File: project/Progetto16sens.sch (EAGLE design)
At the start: 148 parts, among them IC1 LMZ14202TZE-ADJ_NOPB, J2 455-1750-1-ND, M1 43650-0201, M2 43650-0201, M3 43650-0201, M4 43650-0201, M5 ARDUINO-PRO-MINI, SW1 TL32PO, SW2 TL32PO, SW3 TL32PO

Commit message: turned in elaborato
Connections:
- removed net N$1: CB2.1, RB2.2, S5.OUT, S6.VCC, S7.OUT, S8.VCC
- removed net N$2: CB1.1, RB1.2, S1.OUT, S2.VCC, S3.OUT, S4.VCC
- removed net N$3: CB3.1, RB3.2, S10.VCC, S11.OUT, S12.VCC, S9.OUT
- removed net N$4: CB4.1, RB4.2, S13.OUT, S14.VCC, S15.OUT, S16.VCC
- removed net N$69: SV1.12, SV3.10, SV6.11, U$1.GND, U$1.GND_1, U$1.GND_2
- new net PWR_B1: CB1.1, RB1.2, S1.VCC, S2.VCC, S3.VCC, S4.VCC
- new net PWR_B2: CB2.1, RB2.2, S5.VCC, S6.VCC, S7.VCC, S8.VCC
- new net PWR_B3: CB3.1, RB3.2, S10.VCC, S11.VCC, S12.VCC, S9.VCC
- new net PWR_B4: CB4.1, RB4.2, S13.VCC, S14.VCC, S15.VCC, S16.VCC
- net B1: now also S1.OUT; no longer S1.VCC
- net B11: now also S11.OUT; no longer S11.VCC
- net B13: now also S13.OUT; no longer S13.VCC
- net B15: now also S15.OUT; no longer S15.VCC
- net B3: now also S3.OUT; no longer S3.VCC
- net B5: now also S5.OUT; no longer S5.VCC
- net B7: now also S7.OUT; no longer S7.VCC
- net B9: now also S9.OUT; no longer S9.VCC
- net GND: now also SV1.12, SV3.10, SV6.11, U$1.GND, U$1.GND_1, U$1.GND_2
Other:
- moved on the sheet: S1, S11, S13, S15, S3, S5, S7, S9

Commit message: continuing brd
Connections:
- removed net N$13: L_SW2.A, R_SW2.1
- removed net N$15: R_SW2.2, SW2.S
- removed net N$16: L_SW3.A, R_SW3.1
- removed net N$17: R_SW3.2, SW3.S
- removed net N$5: L_SW1.A, R_SW1.1
- removed net N$8: R_SW1.2, SW1.S
- removed net N$81: J1.6, M5.VCC
- new net N$1: L_SW2.C, R_SW2.2
- new net N$2: L_SW1.C, R_SW1.2
- new net N$3: L_SW3.C, R_SW3.2
- net +3V3: now also J1.6, M5.VCC, SW1.S, SW2.S, SW3.S; no longer L_SW1.C, L_SW2.C, L_SW3.C
- net GND: now also R_SW1.1, R_SW2.1, R_SW3.1
- net SW1: now also L_SW1.A
- net SW2: now also L_SW2.A
- net SW3: now also L_SW3.A
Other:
- moved on the sheet: L_SW1, L_SW2, L_SW3, R_SW1, R_SW2, R_SW3, SW1, SW2, SW3

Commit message: halfway done with wiring SEE WIRESTUB ERROR
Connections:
- removed net N$116: J2.2, M5.A6
- removed net N$117: J2.3, M5.A7
- removed net N$61: R_BALL.2, SW_BALL.O
- new net BX: J1.11, M5.D13
- net B1: now also BALL_MUX.I7, J2.3, M5.A7; no longer BALL_MUX.I0, J1.1, M5.A5
- net B10: now also BALL_MUX.I14, M5.D2, SV4.8; no longer BALL_MUX.I9, M5.D9, SV4.1
- net B11: now also BALL_MUX.I13, J1.10, M5.A0; no longer BALL_MUX.I10
- net B12: now also BALL_MUX.I12, J1.9, M5.A1; no longer BALL_MUX.I11, J1.7, M5.A3
- net B13: now also BALL_MUX.I11; no longer BALL_MUX.I12
- net B14: now also BALL_MUX.I10, J1.7, M5.A3; no longer BALL_MUX.I13, J1.9, M5.A1
- net B15: now also BALL_MUX.I9, J1.1, M5.A5; no longer BALL_MUX.I14, J1.10, M5.A0
- net B16: now also BALL_MUX.I8, J1.2, M5.A4; no longer BALL_MUX.I15, J1.11, M5.D13
- net B2: now also BALL_MUX.I6, J2.2, M5.A6; no longer BALL_MUX.I1, J1.2, M5.A4
- net B3: now also BALL_MUX.I5, M5.D9, SV4.1; no longer BALL_MUX.I2, M5.D2, SV4.8
- net B4: now also BALL_MUX.I4, M5.D8, SV4.2; no longer BALL_MUX.I3, M5.D3, SV4.7
- net B5: now also BALL_MUX.I3, M5.D7, SV4.3; no longer BALL_MUX.I4, M5.D4, SV4.6
- net B6: now also BALL_MUX.I2, M5.D6, SV4.4; no longer BALL_MUX.I5, M5.D5, SV4.5
- net B7: now also BALL_MUX.I1, M5.D5, SV4.5; no longer BALL_MUX.I6, M5.D6, SV4.4
- net B8: now also BALL_MUX.I0, M5.D4, SV4.6; no longer BALL_MUX.I7, M5.D7, SV4.3
- net B9: now also BALL_MUX.I15, M5.D3, SV4.7; no longer BALL_MUX.I8, M5.D8, SV4.2
- net E_IN: now also SV6.3, U$1.17/A3/TX4/SDA1; no longer SV6.2, U$1.16/A2/RX4/SCL1
- net E_OUT: now also SV6.2, U$1.16/A2/RX4/SCL1; no longer SV6.3, U$1.17/A3/TX4/SDA1
- net N_IN: now also SV6.5, U$1.19/A5/SCL; no longer SV6.4, U$1.18/A4/SDA
- net N_OUT: now also SV6.4, U$1.18/A4/SDA; no longer SV6.5, U$1.19/A5/SCL
- net S_IN: now also SV6.1, U$1.15/A1/TX3; no longer SV3.12, U$1.14/A0/TX3
- net S_OUT: now also SV3.12, U$1.14/A0/TX3; no longer SV6.1, U$1.15/A1/TX3
- net W_IN: now also SV3.9, U$1.41/A17; no longer SV3.8, U$1.40/A16
- net W_OUT: now also SV3.8, U$1.40/A16; no longer SV3.9, U$1.41/A17

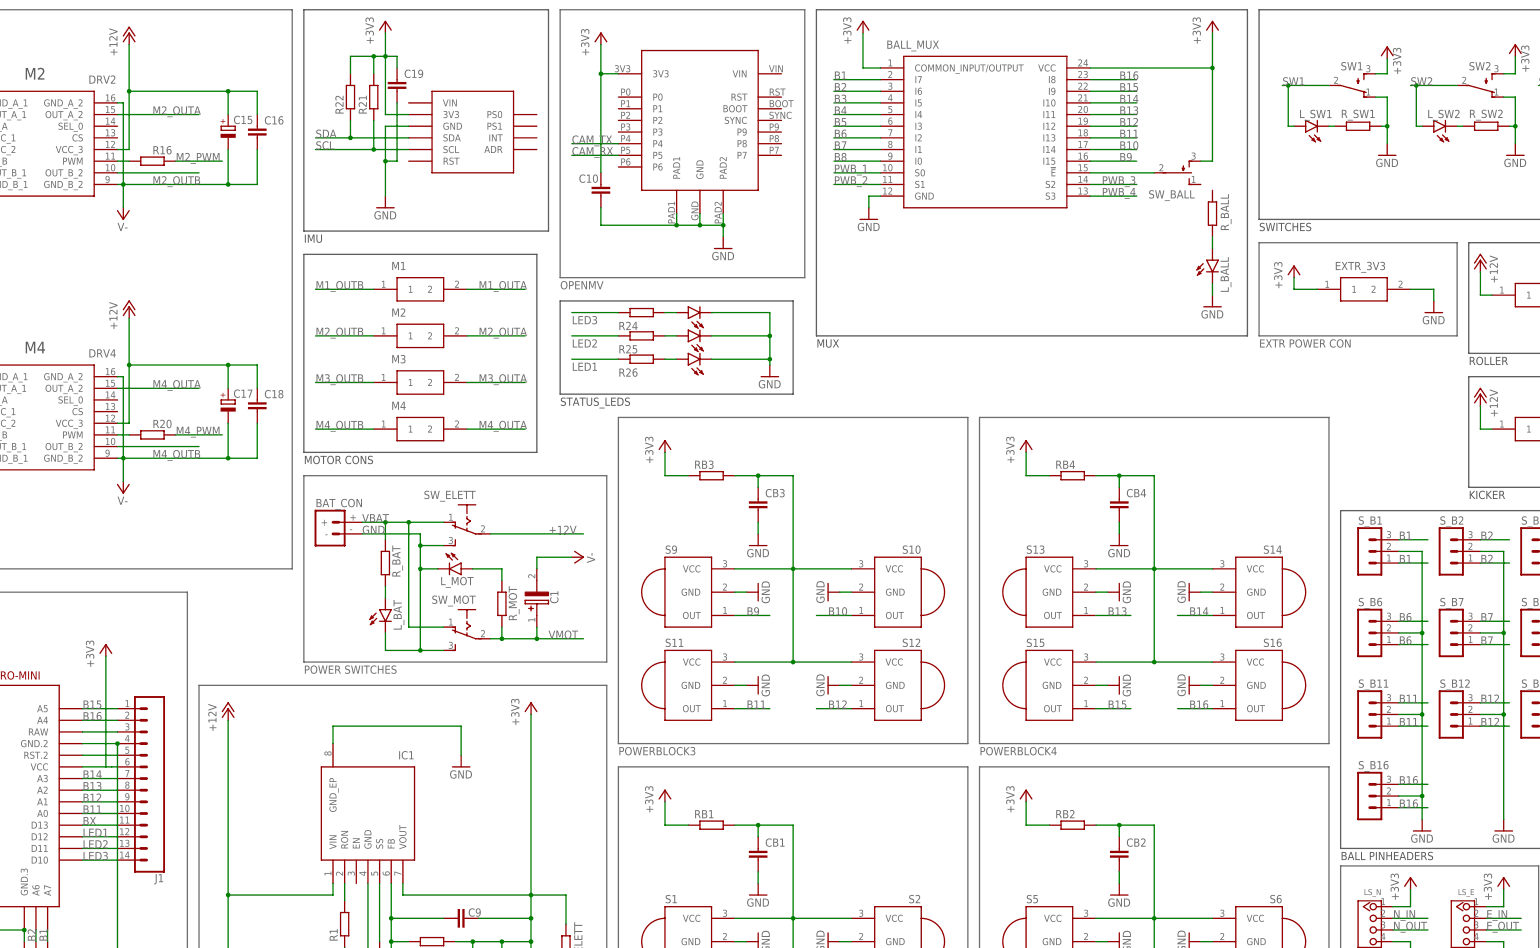
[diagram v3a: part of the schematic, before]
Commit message: elaborato almost done, board needs some fixing
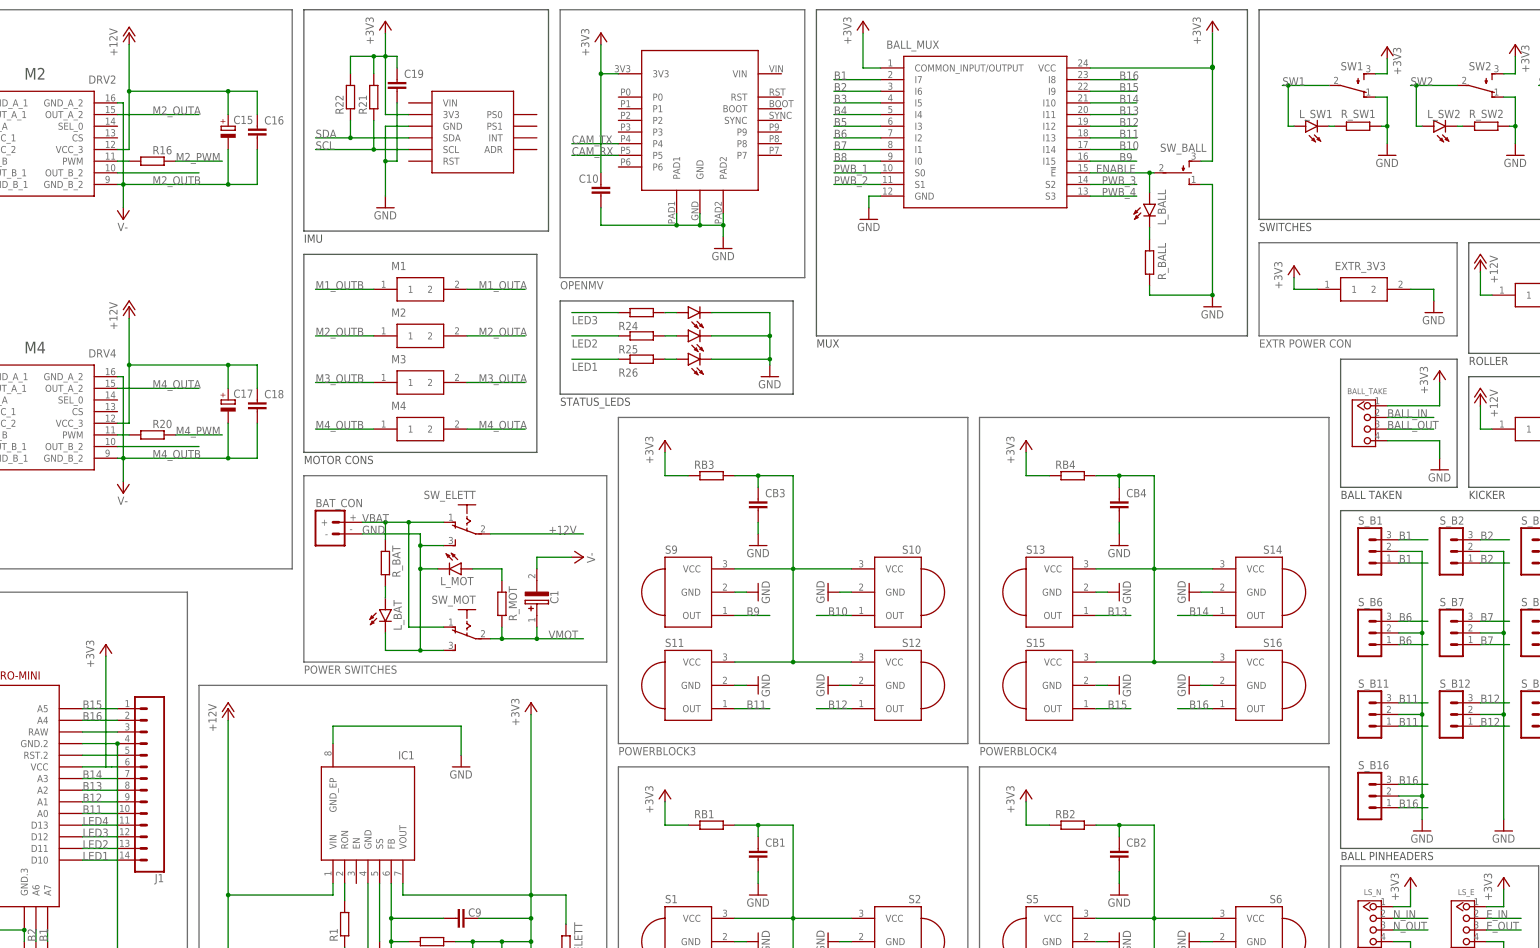
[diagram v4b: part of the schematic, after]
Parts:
- added BALL_TAKE: 4P-2.0, OPL_Connector:GROVE-CONNECTOR-DIP(4P-2.0)
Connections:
- net BX renamed LED4
- removed net N$60: BALL_MUX.!E, SW_BALL.P
- removed net N$62: L_BALL.A, R_BALL.1
- new net ENABLE: BALL_MUX.!E, L_BALL.A, SW_BALL.P
- new net N$8: L_BALL.C, R_BALL.2
- net +3V3: now also BALL_TAKE.1
- net BALL_IN: now also BALL_TAKE.2
- net BALL_OUT: now also BALL_TAKE.3
- net GND: now also BALL_TAKE.4, R_BALL.1, SW_BALL.O; no longer L_BALL.C
- net LED1: now also J1.14, M5.D10; no longer J1.12, M5.D12
- net LED3: now also J1.12, M5.D12; no longer J1.14, M5.D10
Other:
- note added: "BALL TAKEN"
- moved on the sheet: L_BALL, R_BALL
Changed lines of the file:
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@@
 <setting verticaltext="up"/>
 </settings>
-<grid distance="0.1" unitdist="inch" unit="inch" style="lines" multiple="1" display="no" altdistance="0.01" altunitdist="inch" altunit="inch"/>
+<grid distance="0.1" unitdist="inch" unit="inch" style="lines" multiple="1" display="yes" altdistance="0.05" altunitdist="inch" altunit="inch"/>
 <layers>
 <layer number="1" name="Top" color="4" fill="1" visible="no" active="no"/>
@@
 <part name="GND50" library="supply1" library_urn="urn:adsk.eagle:library:371" deviceset="GND" device=""/>
 <part name="+3V22" library="supply1" library_urn="urn:adsk.eagle:library:371" deviceset="+3V3" device=""/>
+<part name="BALL_TAKE" library="OPL_Connector" deviceset="GROVE-CONNECTOR-DIP(4P-2.0)" device="" package3d_urn="urn:adsk.eagle:package:8004548/1" value="4P-2.0"/>
+<part name="GND51" library="supply1" library_urn="urn:adsk.eagle:library:371" deviceset="GND" device=""/>
+<part name="+3V23" library="supply1" library_urn="urn:adsk.eagle:library:371" deviceset="+3V3" device=""/>
 </parts>
 <sheets>
@@
 <text x="474.98" y="132.08" size="1.778" layer="97">KICKER</text>
 <text x="0" y="236.22" size="1.778" layer="97">*in motors the value is VMOT</text>
+<wire x1="447.04" y1="162.56" x2="447.04" y2="134.62" width="0.1524" layer="97"/>
+<wire x1="447.04" y1="134.62" x2="472.44" y2="134.62" width="0.1524" layer="97"/>
+<wire x1="472.44" y1="134.62" x2="472.44" y2="162.56" width="0.1524" layer="97"/>
+<wire x1="472.44" y1="162.56" x2="447.04" y2="162.56" width="0.1524" layer="97"/>
+<text x="447.04" y="132.08" size="1.778" layer="97">BALL TAKEN</text>
 </plain>
 <instances>
@@
 </instance>
 <instance part="SW_BALL" gate="BEF1" x="411.48" y="203.2" smashed="yes" rot="MR90">
-<attribute name="NAME" x="405.13" y="199.39" size="1.778" layer="95" rot="MR180"/>
+<attribute name="NAME" x="407.67" y="209.55" size="1.778" layer="95" rot="MR180"/>
 </instance>
 <instance part="GND22" gate="1" x="419.1" y="173.99" smashed="yes">
 <attribute name="VALUE" x="416.56" y="171.45" size="1.778" layer="96"/>
 </instance>
-<instance part="L_BALL" gate="G$1" x="419.1" y="184.15" smashed="yes">
-<attribute name="NAME" x="422.656" y="177.038" size="1.778" layer="95" rot="R90"/>
-<attribute name="VALUE" x="424.815" y="179.578" size="1.778" layer="96" rot="R90"/>
-</instance>
-<instance part="R_BALL" gate="G$1" x="419.1" y="194.31" smashed="yes" rot="R90">
-<attribute name="NAME" x="422.6814" y="190.5" size="1.778" layer="95" rot="R90"/>
-<attribute name="VALUE" x="422.402" y="190.5" size="1.778" layer="96" rot="R90"/>
+<instance part="L_BALL" gate="G$1" x="405.384" y="196.342" smashed="yes">
+<attribute name="NAME" x="408.94" y="191.77" size="1.778" layer="95" rot="R90"/>
+<attribute name="VALUE" x="411.099" y="191.77" size="1.778" layer="96" rot="R90"/>
+</instance>
+<instance part="R_BALL" gate="G$1" x="405.384" y="183.642" smashed="yes" rot="R90">
+<attribute name="NAME" x="408.9654" y="179.832" size="1.778" layer="95" rot="R90"/>
+<attribute name="VALUE" x="408.686" y="179.832" size="1.778" layer="96" rot="R90"/>
 </instance>
 <instance part="U$1" gate="G$1" x="45.72" y="59.69" smashed="yes"/>
@@
 <attribute name="VALUE" x="175.26" y="95.25" size="1.778" layer="96" rot="R90"/>
 </instance>
+<instance part="BALL_TAKE" gate="G$1" x="453.39" y="148.59" smashed="yes" rot="MR0">
+<attribute name="NAME" x="457.2" y="154.94" size="1.27" layer="95" ratio="10" rot="MR0"/>
+</instance>
+<instance part="GND51" gate="1" x="468.63" y="138.43" smashed="yes">
+<attribute name="VALUE" x="466.09" y="135.89" size="1.778" layer="96"/>
+</instance>
+<instance part="+3V23" gate="G$1" x="468.63" y="160.02" smashed="yes">
+<attribute name="VALUE" x="466.09" y="154.94" size="1.778" layer="96" rot="R90"/>
+</instance>
 </instances>
 <busses>
@@
 </segment>
 <segment>
-<pinref part="GND22" gate="1" pin="GND"/>
-<pinref part="L_BALL" gate="G$1" pin="C"/>
-<wire x1="419.1" y1="176.53" x2="419.1" y2="179.07" width="0.1524" layer="91"/>
-</segment>
-<segment>
 <pinref part="S_B1" gate="G$1" pin="2"/>
 <wire x1="459.74" y1="120.65" x2="464.82" y2="120.65" width="0.1524" layer="91"/>
@@
 <junction x="76.2" y="83.82"/>
 </segment>
+<segment>
+<pinref part="GND22" gate="1" pin="GND"/>
+<pinref part="SW_BALL" gate="BEF1" pin="O"/>
+<wire x1="416.56" y1="200.66" x2="419.1" y2="200.66" width="0.1524" layer="91"/>
+<wire x1="419.1" y1="200.66" x2="419.1" y2="176.53" width="0.1524" layer="91"/>
+<junction x="419.1" y="176.53"/>
+<pinref part="R_BALL" gate="G$1" pin="1"/>
+<wire x1="405.384" y1="178.562" x2="405.384" y2="176.53" width="0.1524" layer="91"/>
+<wire x1="405.384" y1="176.53" x2="419.1" y2="176.53" width="0.1524" layer="91"/>
+</segment>
+<segment>
+<pinref part="BALL_TAKE" gate="G$1" pin="4"/>
+<wire x1="457.2" y1="144.78" x2="468.63" y2="144.78" width="0.1524" layer="91"/>
+<wire x1="468.63" y1="144.78" x2="468.63" y2="140.97" width="0.1524" layer="91"/>
+<pinref part="GND51" gate="1" pin="GND"/>
+</segment>
 </net>
 <net name="+3V3" class="0">
@@
 <wire x1="392.43" y1="226.06" x2="419.1" y2="226.06" width="0.1524" layer="91"/>
 <pinref part="+3V5" gate="G$1" pin="+3V3"/>
-<wire x1="419.1" y1="226.06" x2="419.1" y2="233.68" width="0.1524" layer="91"/>
+<wire x1="419.1" y1="226.06" x2="419.1" y2="226.314" width="0.1524" layer="91"/>
+<wire x1="419.1" y1="226.314" x2="419.1" y2="233.68" width="0.1524" layer="91"/>
+<wire x1="419.354" y1="226.314" x2="419.1" y2="226.314" width="0.1524" layer="91"/>
+<junction x="419.1" y="226.314"/>
 <pinref part="SW_BALL" gate="BEF1" pin="S"/>
 <wire x1="416.56" y1="205.74" x2="419.1" y2="205.74" width="0.1524" layer="91"/>
-<wire x1="419.1" y1="205.74" x2="419.1" y2="226.06" width="0.1524" layer="91"/>
+<wire x1="419.1" y1="226.06" x2="419.1" y2="205.74" width="0.1524" layer="91"/>
 <junction x="419.1" y="226.06"/>
 </segment>
@@
 <wire x1="177.8" y1="73.66" x2="177.8" y2="97.79" width="0.1524" layer="91"/>
 </segment>
+<segment>
+<pinref part="BALL_TAKE" gate="G$1" pin="1"/>
+<wire x1="457.2" y1="152.4" x2="468.63" y2="152.4" width="0.1524" layer="91"/>
+<wire x1="468.63" y1="152.4" x2="468.63" y2="157.48" width="0.1524" layer="91"/>
+<pinref part="+3V23" gate="G$1" pin="+3V3"/>
+</segment>
 </net>
 <net name="PWR_B3" class="0">
@@
 </segment>
 </net>
-<net name="N$60" class="0">
-<segment>
-<pinref part="BALL_MUX" gate="G$1" pin="!E"/>
-<pinref part="SW_BALL" gate="BEF1" pin="P"/>
-<wire x1="392.43" y1="203.2" x2="406.4" y2="203.2" width="0.1524" layer="91"/>
-</segment>
-</net>
-<net name="N$62" class="0">
-<segment>
-<pinref part="L_BALL" gate="G$1" pin="A"/>
-<pinref part="R_BALL" gate="G$1" pin="1"/>
-<wire x1="419.1" y1="186.69" x2="419.1" y2="189.23" width="0.1524" layer="91"/>
-</segment>
-</net>
 <net name="R_DIG" class="0">
 <segment>
@@
 <label x="78.74" y="53.34" size="1.778" layer="95"/>
 </segment>
+<segment>
+<pinref part="BALL_TAKE" gate="G$1" pin="2"/>
+<wire x1="457.2" y1="149.86" x2="467.36" y2="149.86" width="0.1524" layer="91"/>
+<label x="457.2" y="149.86" size="1.778" layer="95"/>
+</segment>
 </net>
 <net name="N$65" class="0">
@@
 <label x="78.74" y="27.94" size="1.778" layer="95"/>
 </segment>
+<segment>
+<pinref part="BALL_TAKE" gate="G$1" pin="3"/>
+<wire x1="457.2" y1="147.32" x2="467.36" y2="147.32" width="0.1524" layer="91"/>
+<label x="457.2" y="147.32" size="1.778" layer="95"/>
+</segment>
 </net>
 <net name="A_TX" class="0">
@@
 <net name="LED1" class="0">
 <segment>
-<pinref part="M5" gate="G$1" pin="D12"/>
-<pinref part="J1" gate="G$1" pin="12"/>
-<wire x1="172.72" y1="58.42" x2="180.34" y2="58.42" width="0.1524" layer="91"/>
-<label x="172.72" y="58.42" size="1.778" layer="95"/>
-</segment>
-<segment>
 <wire x1="289.56" y1="162.56" x2="279.4" y2="162.56" width="0.1524" layer="91"/>
 <pinref part="R26" gate="G$1" pin="1"/>
 <label x="279.4" y="160.02" size="1.778" layer="95"/>
 </segment>
+<segment>
+<pinref part="M5" gate="G$1" pin="D10"/>
+<pinref part="J1" gate="G$1" pin="14"/>
+<wire x1="172.72" y1="53.34" x2="180.34" y2="53.34" width="0.1524" layer="91"/>
+<label x="172.72" y="53.34" size="1.778" layer="95"/>
+</segment>
 </net>
 <net name="LED2" class="0">
@@
 <net name="LED3" class="0">
 <segment>
-<pinref part="M5" gate="G$1" pin="D10"/>
-<pinref part="J1" gate="G$1" pin="14"/>
-<wire x1="172.72" y1="53.34" x2="180.34" y2="53.34" width="0.1524" layer="91"/>
-<label x="172.72" y="53.34" size="1.778" layer="95"/>
-</segment>
-<segment>
 <wire x1="289.56" y1="172.72" x2="279.4" y2="172.72" width="0.1524" layer="91"/>
 <pinref part="R24" gate="G$1" pin="1"/>
 <label x="279.4" y="170.18" size="1.778" layer="95"/>
 </segment>
+<segment>
+<pinref part="M5" gate="G$1" pin="D12"/>
+<pinref part="J1" gate="G$1" pin="12"/>
+<wire x1="172.72" y1="58.42" x2="180.34" y2="58.42" width="0.1524" layer="91"/>
+<label x="172.72" y="58.42" size="1.778" layer="95"/>
+</segment>
 </net>
 <net name="N$20" class="0">
@@
 </segment>
 </net>
-<net name="BX" class="0">
+<net name="LED4" class="0">
 <segment>
 <pinref part="J1" gate="G$1" pin="11"/>
@@
 </segment>
 </net>
+<net name="ENABLE" class="0">
+<segment>
+<pinref part="SW_BALL" gate="BEF1" pin="P"/>
+<pinref part="BALL_MUX" gate="G$1" pin="!E"/>
+<wire x1="392.43" y1="203.2" x2="405.384" y2="203.2" width="0.1524" layer="91"/>
+<pinref part="L_BALL" gate="G$1" pin="A"/>
+<wire x1="405.384" y1="203.2" x2="406.4" y2="203.2" width="0.1524" layer="91"/>
+<wire x1="405.384" y1="198.882" x2="405.384" y2="203.2" width="0.1524" layer="91"/>
+<junction x="405.384" y="203.2"/>
+<label x="393.7" y="203.2" size="1.778" layer="95"/>
+</segment>
+</net>
+<net name="N$8" class="0">
+<segment>
+<pinref part="L_BALL" gate="G$1" pin="C"/>
+<pinref part="R_BALL" gate="G$1" pin="2"/>
+<wire x1="405.384" y1="191.262" x2="405.384" y2="188.722" width="0.1524" layer="91"/>
+</segment>
+</net>

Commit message: BOARD IS DONE EVEN IF IT HAS SOME ZOZZATE and some drill size drc errors but what can u do nowadays
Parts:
- added C21: (no value), rcl:C-EUC1206
- added C22, C23: (no value), rcl:C-EUC0805
- added LED4: (no value), led:LEDCHIPLED_1206
- added R4: (no value), rcl:R-EU_R0805
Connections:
- removed net N$65: J1.3, M5.RAW
- removed net N$68: J1.5, M5.RST.2
- removed net N$85: M5.RST.1, SV4.10
- new net N$4: LED4.A, R4.2
- net +3V3: now also C21.1, C22.1, C23.1
- net GND: now also C21.2, C22.2, C23.2, LED4.C
- net LED4: now also R4.1
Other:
- moved on the sheet: R24, R25, R26
